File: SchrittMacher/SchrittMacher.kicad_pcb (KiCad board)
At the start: 2 copper layers, 99.7 x 71.5 mm, 90 parts, among them CON1 BARREL_JACK, J1 JACK_2P, J2 JACK_2P, J3 JACK_2P, J4 JACK_2P, Q1 BC547, Q10 BC547, Q2 BC547, Q3 BC547, Q4 BC547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

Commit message: more silkscreen
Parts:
- added G***: LOGO, kicad-cbase:c-base, F.Cu at (167.3, 106.0)
- added G***: LOGO, kicad-cbase:c-base-logo-ceva, F.Cu at (103.9, 103.7)
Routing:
- net /Steps/STEP-IN-6: track 69.4 -> 51.9 mm
- net /Steps/STEP-IN-9: track 83.9 -> 86.7 mm
- net /Steps/STEP-IN-8: track 113.9 -> 116.6 mm
- net Net-(C2-Pad1): track 28.1 -> 25.9 mm
- net /ClockGenerator/CLOCK: track 43.2 -> 42.5 mm, vias 2 -> 1
- added copper zone on F.Cu, net GND
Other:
- board text added: "555"
- board text added: "CD4017"
- board text added: "CV-Out"
- board text added: "Clock-Speed"
- board text added: "Gate-In"
- board text added: "Gate-Out"
- board text added: "TL072"
- board text added: "c_rittmacher v1.0"
- board text added: "woodworker@c-base.org"

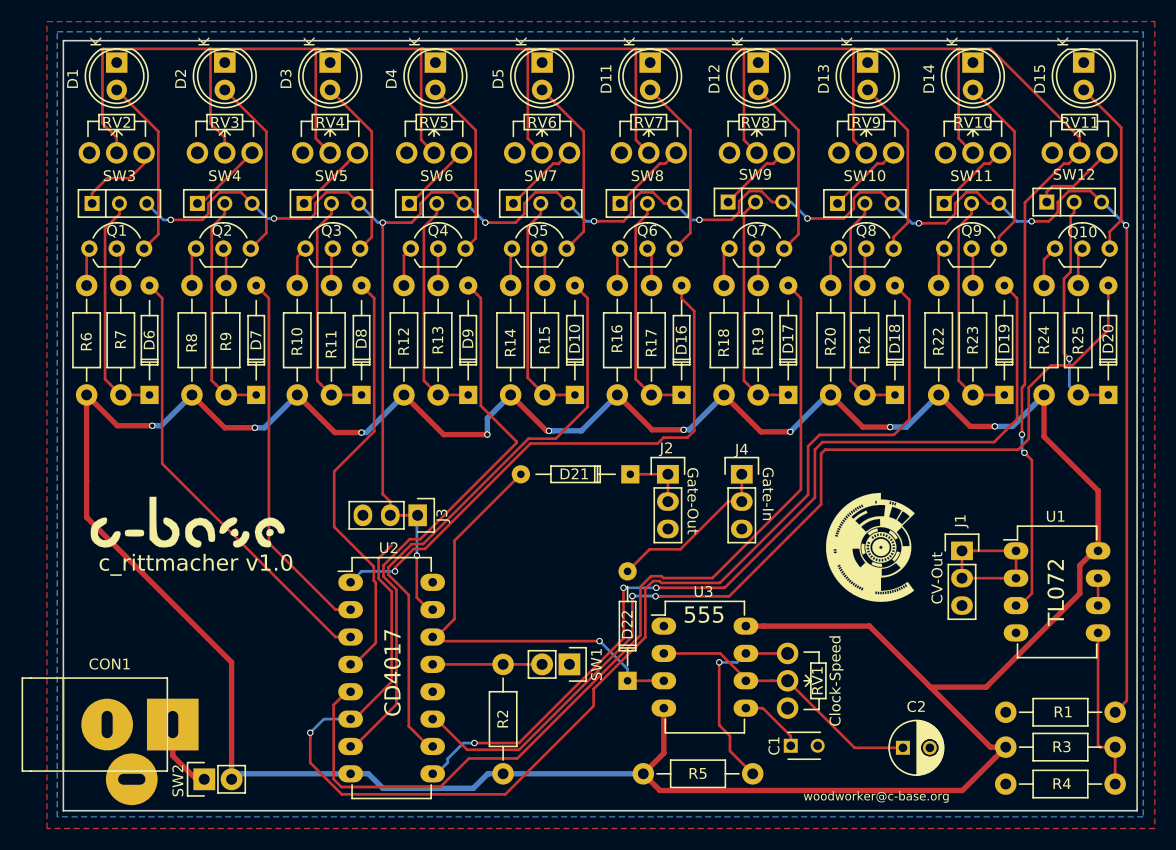
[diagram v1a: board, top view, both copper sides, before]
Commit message: fixed some circuit problems in schrittmacher
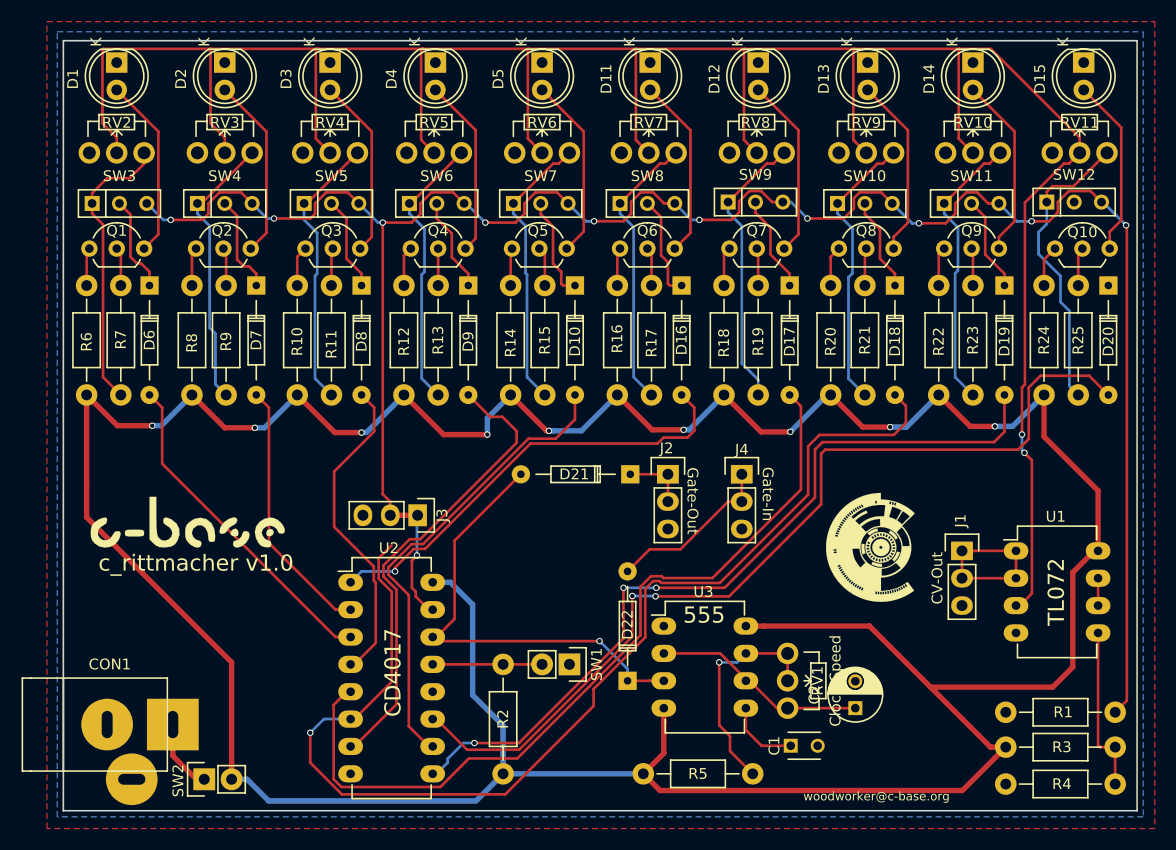
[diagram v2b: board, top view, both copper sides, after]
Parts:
- moved D17 10.2 mm to (159.8, 81.7), turned to 270 degrees
- moved D18 10.2 mm to (169.5, 81.7), turned to 270 degrees
- moved D6 10.2 mm to (100.3, 81.7), turned to 270 degrees
- moved D7 10.2 mm to (110.2, 81.7), turned to 270 degrees
- moved D9 10.2 mm to (129.9, 81.7), turned to 270 degrees
- moved D16 10.2 mm to (149.7, 81.7), turned to 270 degrees
- moved D20 10.2 mm to (189.4, 81.7), turned to 270 degrees
- moved D8 10.2 mm to (120.0, 81.7), turned to 270 degrees
- moved D10 10.2 mm to (139.8, 81.7), turned to 270 degrees
- moved D19 10.2 mm to (179.7, 81.7), turned to 270 degrees
- moved C2 5.75 mm to (165.9, 120.9), turned to 90 degrees
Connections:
- net /ClockGenerator/CLOCK renamed /CLOCK
- net /Steps/RESET renamed /RESET
- R11 pad 2: Net-(D8-Pad1) -> Net-(R11-Pad2)
- R13 pad 2: Net-(D9-Pad1) -> Net-(R13-Pad2)
- R15 pad 2: Net-(D10-Pad1) -> Net-(R15-Pad2)
- R17 pad 2: Net-(D16-Pad1) -> Net-(R17-Pad2)
- R19 pad 2: Net-(D17-Pad1) -> Net-(R19-Pad2)
- R21 pad 2: Net-(D18-Pad1) -> Net-(R21-Pad2)
- R23 pad 2: Net-(D19-Pad1) -> Net-(R23-Pad2)
- R25 pad 2: Net-(D20-Pad1) -> Net-(R25-Pad2)
- R7 pad 2: Net-(D6-Pad1) -> Net-(R7-Pad2)
- R9 pad 2: Net-(D7-Pad1) -> Net-(R9-Pad2)
- RV1 pad 2: Net-(C2-Pad1) -> Net-(R5-Pad2)
- RV1 pad 3: GND -> Net-(C2-Pad1)
- RV10 pad 3: Net-(RV10-Pad3) -> Net-(R23-Pad2)
- RV11 pad 3: Net-(RV11-Pad3) -> Net-(R25-Pad2)
- RV2 pad 3: Net-(RV2-Pad3) -> Net-(R7-Pad2)
- RV3 pad 3: Net-(RV3-Pad3) -> Net-(R9-Pad2)
- RV4 pad 3: Net-(RV4-Pad3) -> Net-(R11-Pad2)
- RV5 pad 3: Net-(RV5-Pad3) -> Net-(R13-Pad2)
- RV6 pad 3: Net-(RV6-Pad3) -> Net-(R15-Pad2)
- RV7 pad 3: Net-(RV7-Pad3) -> Net-(R17-Pad2)
- RV8 pad 3: Net-(RV8-Pad3) -> Net-(R19-Pad2)
- RV9 pad 3: Net-(RV9-Pad3) -> Net-(R21-Pad2)
- SW10 pad 1: Net-(RV9-Pad3) -> Net-(R21-Pad2)
- SW11 pad 1: Net-(RV10-Pad3) -> Net-(R23-Pad2)
- SW12 pad 1: Net-(RV11-Pad3) -> Net-(R25-Pad2)
- SW3 pad 1: Net-(RV2-Pad3) -> Net-(R7-Pad2)
- SW4 pad 1: Net-(RV3-Pad3) -> Net-(R9-Pad2)
- SW5 pad 1: Net-(RV4-Pad3) -> Net-(R11-Pad2)
- SW6 pad 1: Net-(RV5-Pad3) -> Net-(R13-Pad2)
- SW7 pad 1: Net-(RV6-Pad3) -> Net-(R15-Pad2)
- SW8 pad 1: Net-(RV7-Pad3) -> Net-(R17-Pad2)
- SW9 pad 1: Net-(RV8-Pad3) -> Net-(R19-Pad2)
- U2 pad 16: GND -> VCC
- U2 pad 8: VCC -> GND
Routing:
- net Net-(R25-Pad2): track 0.00 -> 27.8 mm
- net Net-(R7-Pad2): track 0.00 -> 26.8 mm
- net VCC: track 305.1 -> 331.5 mm
- net Net-(R21-Pad2): track 0.00 -> 26.3 mm
- net Net-(R23-Pad2): track 0.00 -> 26.2 mm
- net Net-(R19-Pad2): track 0.00 -> 26.2 mm
- net Net-(R15-Pad2): track 0.00 -> 26.1 mm
- net Net-(R17-Pad2): track 0.00 -> 26.1 mm
- net Net-(R9-Pad2): track 0.00 -> 25.9 mm
- net Net-(R11-Pad2): track 0.00 -> 25.9 mm
- net Net-(R13-Pad2): track 0.00 -> 25.9 mm
- net Net-(D20-Pad1): track 21.6 -> 0.00 mm, vias 1 -> 0
- net Net-(D18-Pad1): track 21.7 -> 8.78 mm
- net Net-(D8-Pad1): track 21.7 -> 8.78 mm
- net Net-(D19-Pad1): track 21.7 -> 8.89 mm
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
